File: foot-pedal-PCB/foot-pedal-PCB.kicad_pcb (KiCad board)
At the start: 2 copper layers, 19 parts, among them J1 1-726388-2, J2 1-726388-2, J3 Conn_01x01_Pin, J4 Conn_01x01_Pin, J5 Conn_01x01_Pin, J6 Conn_01x01_Pin, J7 Conn_01x01_Pin, Q1 BT137-600E

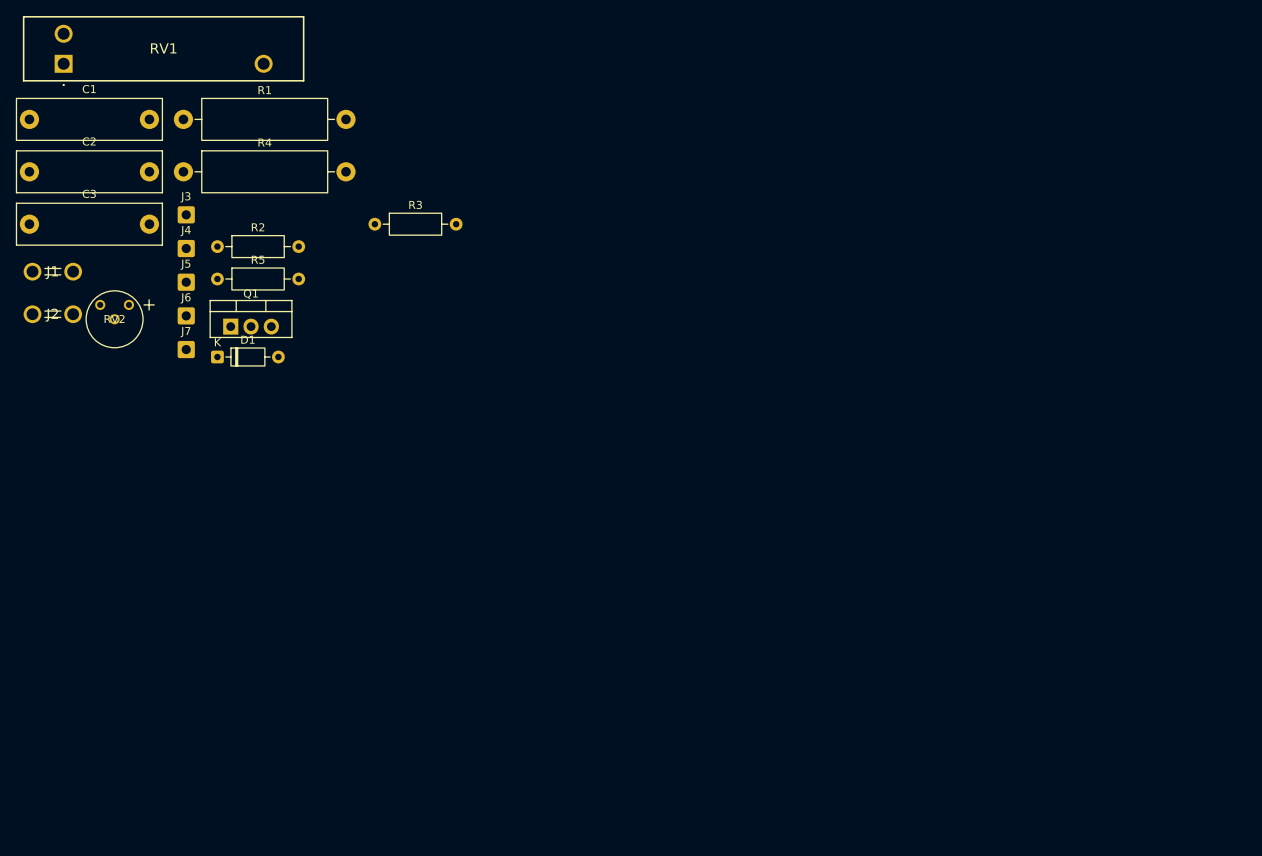
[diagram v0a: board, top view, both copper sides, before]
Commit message: Added circuit protection, finished foot pedal PCB design, ordered from OSHPark
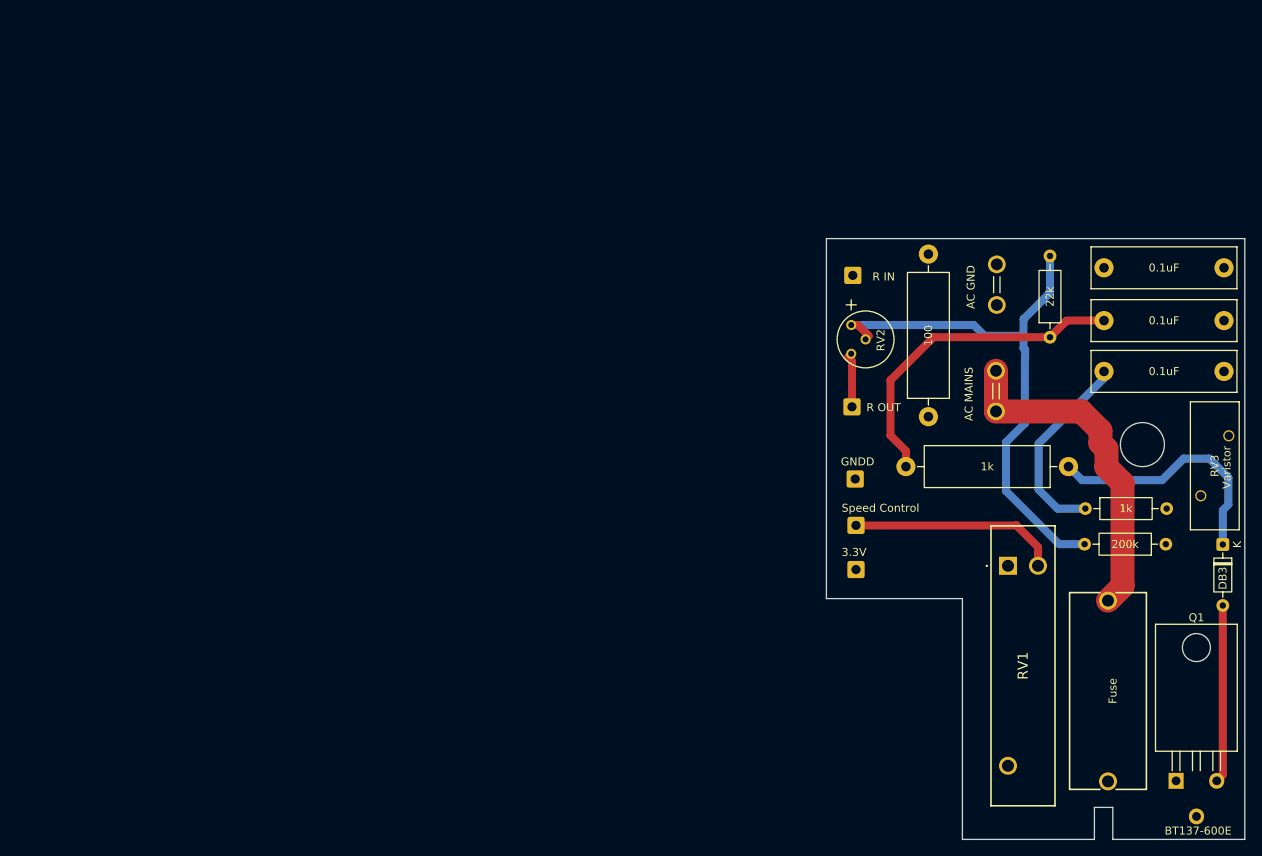
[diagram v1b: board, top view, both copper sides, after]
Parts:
- added H1: MountingHole, MountingHole:MountingHole_5.5mm, F.Cu at (166.6, 76.5)
- added J8: Fuse, project:696108003002, F.Cu at (162.3, 107.2)
- added RV3: Varistor, project:VAR_B72214P2301K101, F.Cu at (175.7, 79.1)
- Q1: footprint Package_TO_SOT_THT:TO-220-3_Vertical -> project:BT137-600E
- moved C1 152.6 mm to (176.8, 67.3), turned to 180 degrees
- moved C2 150.5 mm to (176.8, 61.0), turned to 180 degrees
- moved C3 149.4 mm to (176.8, 54.4), turned to 180 degrees
- moved RV1 133.7 mm to (149.8, 91.6), turned to -90 degrees
- moved Q1 131.1 mm to (170.8, 118.5)
- moved D1 127.8 mm to (176.7, 88.9), turned to -90 degrees
- moved R5 123.1 mm to (169.5, 88.9), turned to 180 degrees
- moved R1 118.8 mm to (157.4, 79.2), turned to 180 degrees
- moved J1 118.8 mm to (148.3, 69.8), turned to 90 degrees
- moved J2 118.1 mm to (148.4, 56.5), turned to 90 degrees
- moved R2 104.7 mm to (155.1, 63.0), turned to 90 degrees
- moved R4 98.0 mm to (139.8, 73.0), turned to 90 degrees
- moved R3 95.7 mm to (159.5, 84.5)
- moved RV2 90.3 mm to (130.2, 61.5), turned to 90 degrees
- moved J7 88.1 mm to (130.8, 92.1)
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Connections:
- J1 pad 1: AC -> Net-(J1-Pad1)
- J1 pad 2: AC -> Net-(J1-Pad1)
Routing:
- net AC: track 0.00 -> 124.1 mm
- net Net-(R2-Pad2): track 0.00 -> 69.3 mm
- net Net-(J1-Pad1): track 0.00 -> 42.3 mm
- net Net-(C2-Pad2): track 0.00 -> 41.4 mm
- net +3.3V: track 0.00 -> 40.4 mm
- net Net-(C3-Pad2): track 0.00 -> 31.9 mm
- net Net-(D1-K): track 0.00 -> 31.4 mm
- net Net-(J6-Pin_1): track 0.00 -> 26.2 mm
- net Net-(C1-Pad2): track 0.00 -> 25.0 mm
- net Net-(D1-A): track 0.00 -> 22.2 mm
- net /Res_out: track 0.00 -> 6.43 mm
- added copper zone on In1.Cu, net GND
- added copper zone on In1.Cu, net GNDD
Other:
- board outline added: 52.3 x 75.1 mm
- copper layers 2 -> 4
- board text added: "3.3V"
- board text added: "AC GND"
- board text added: "AC MAINS"
- board text added: "GNDD"
- board text added: "R IN"
- board text added: "R OUT"
- board text added: "Speed Control"
